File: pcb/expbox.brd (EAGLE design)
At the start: 87 x 47 mm, 48 parts, among them IC1 7805TV, K1 G5LE, Q1 2N3904, Q2 2N3904, Q3 2N3904, Q4 2N3904, Q5 2N3904, Q6 2N3904

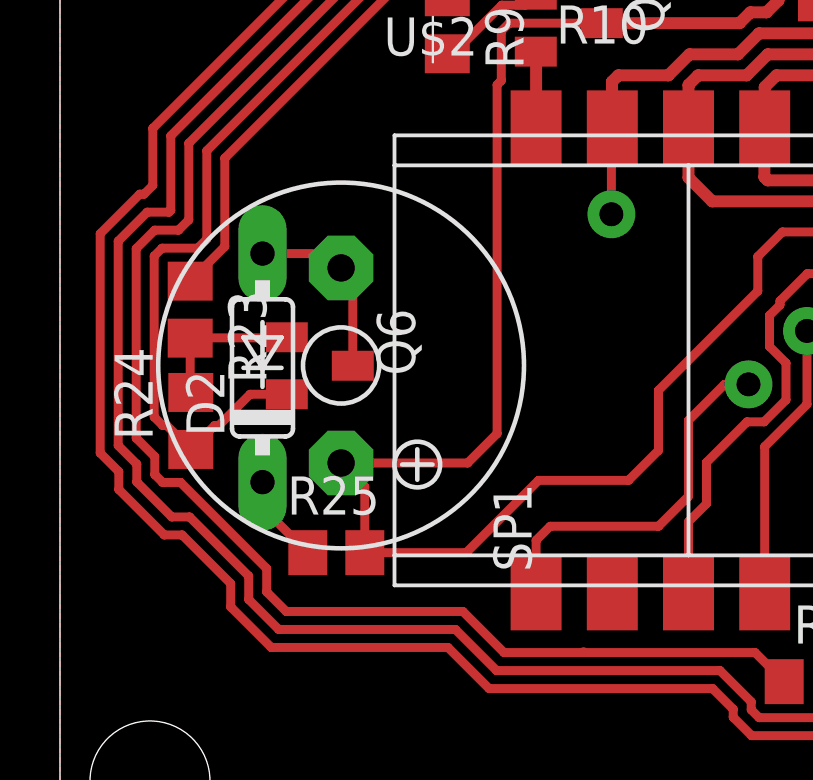
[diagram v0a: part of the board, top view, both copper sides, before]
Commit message: Replace buzzer with one with wider legs
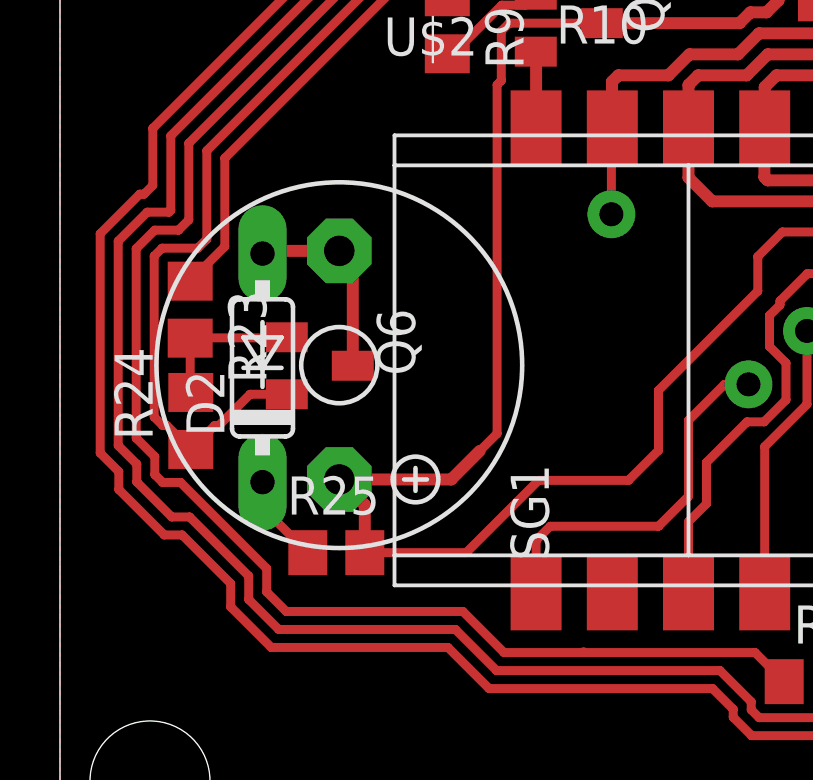
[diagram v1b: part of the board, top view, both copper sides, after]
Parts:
- removed SP1: KSS1201, buzzer:KSS1201
- added SG1: F/TMB, buzzer:F/TMB
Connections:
- net N$21: now also SG1.-; no longer SP1.-
- net VCC: now also SG1.+; no longer SP1.+
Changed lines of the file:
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@@
 <layer number="43" name="vRestrict" color="2" fill="10" visible="no" active="yes"/>
 <layer number="44" name="Drills" color="7" fill="1" visible="no" active="yes"/>
-<layer number="45" name="Holes" color="7" fill="1" visible="no" active="yes"/>
+<layer number="45" name="Holes" color="7" fill="1" visible="yes" active="yes"/>
 <layer number="46" name="Milling" color="3" fill="1" visible="no" active="yes"/>
 <layer number="47" name="Measures" color="7" fill="1" visible="no" active="yes"/>
@@
 <attribute name="VALUE" x="10.37" y="28.825" size="1.27" layer="27" rot="R270"/>
 </element>
-<element name="SP1" library="buzzer" library_urn="urn:adsk.eagle:library:113" package="KSS1201" package3d_urn="urn:adsk.eagle:package:5268/1" value="KSS1201" x="9.37" y="16.85" smashed="yes" rot="R270">
-<attribute name="MF" value="" x="-60.48" y="-30.14" size="1.778" layer="27" rot="R270" display="off"/>
-<attribute name="MPN" value="" x="-60.48" y="-30.14" size="1.778" layer="27" rot="R270" display="off"/>
-<attribute name="NAME" x="14.45" y="12.913" size="1.27" layer="25" ratio="10" rot="R270"/>
-<attribute name="OC_FARNELL" value="unknown" x="-60.48" y="-30.14" size="1.778" layer="27" rot="R270" display="off"/>
-<attribute name="OC_NEWARK" value="unknown" x="-60.48" y="-30.14" size="1.778" layer="27" rot="R270" display="off"/>
-<attribute name="POPULARITY" value="1" x="-60.48" y="-30.14" size="1.778" layer="27" rot="R270" display="off"/>
-<attribute name="VALUE" x="5.56" y="20.406" size="1.27" layer="27" ratio="10" rot="R270"/>
-</element>
 <element name="U$1" library="PIC16F886-I_SP" package="DIP762W46P254L3467H457Q28" value="PIC16F886-I/SP" x="31.95" y="38.02" smashed="yes" rot="MR90">
 <attribute name="AVAILABILITY" value="Good" x="0.2" y="65.96" size="1.778" layer="28" rot="MR90" display="off"/>
@@
 <attribute name="POPULARITY" value="10" x="149.58" y="76.85" size="1.778" layer="27" rot="R90" display="off"/>
 <attribute name="VALUE" x="87.985" y="3.19" size="1.27" layer="27" ratio="10" rot="R90"/>
+</element>
+<element name="SG1" library="buzzer" library_urn="urn:adsk.eagle:library:113" package="F/TMB" package3d_urn="urn:adsk.eagle:package:5260/1" value="F/TMB" x="9.31" y="16.86" smashed="yes" rot="R270">
+<attribute name="MF" value="" x="9.31" y="16.86" size="1.778" layer="27" rot="R270" display="off"/>
+<attribute name="MPN" value="" x="9.31" y="16.86" size="1.778" layer="27" rot="R270" display="off"/>
+<attribute name="NAME" x="15.025" y="13.558" size="1.27" layer="25" ratio="10" rot="R270"/>
+<attribute name="OC_FARNELL" value="unknown" x="9.31" y="16.86" size="1.778" layer="27" rot="R270" display="off"/>
+<attribute name="OC_NEWARK" value="unknown" x="9.31" y="16.86" size="1.778" layer="27" rot="R270" display="off"/>
+<attribute name="POPULARITY" value="1" x="9.31" y="16.86" size="1.778" layer="27" rot="R270" display="off"/>
+<attribute name="VALUE" x="5.5" y="20.67" size="1.27" layer="27" ratio="10" rot="R270"/>
 </element>
 </elements>
@@
 <vertex x="87" y="47"/>
 </polygon>
-<wire x1="31.77" y1="13.62" x2="31.77" y2="9.31" width="0" layer="19" extent="1-1"/>
+<wire x1="31.77" y1="9.31" x2="31.77" y2="13.62" width="0" layer="19" extent="1-1"/>
 </signal>
 <signal name="VCC">
@@
 <contactref element="K1" pad="1"/>
 <contactref element="D1" pad="C"/>
-<contactref element="SP1" pad="+"/>
 <contactref element="R25" pad="2"/>
 <wire x1="63" y1="31.28" x2="63" y2="33.23" width="0.5" layer="1"/>
@@
 <wire x1="28.14" y1="36.28" x2="28.14" y2="39.02" width="0.4" layer="1"/>
 <wire x1="28.14" y1="39.02" x2="28.14" y2="41.83" width="0.4" layer="1"/>
-<wire x1="10.16" y1="10.61" x2="10.16" y2="12.8088" width="0.3" layer="1"/>
-<wire x1="10.16" y1="12.8088" x2="9.37" y2="13.5988" width="0.3" layer="1"/>
 <wire x1="10.16" y1="10.61" x2="13.54" y2="10.61" width="0.3" layer="1"/>
 <wire x1="13.54" y1="10.61" x2="15.95" y2="13.02" width="0.3" layer="1"/>
@@
 <wire x1="14.71" y1="26.34639375" x2="14.57" y2="26.20639375" width="0.3" layer="1"/>
 <wire x1="14.57" y1="26.20639375" x2="14.57" y2="14.58" width="0.3" layer="1"/>
-<wire x1="13.5888" y1="13.5988" x2="9.37" y2="13.5988" width="0.3" layer="1"/>
 <wire x1="14.71" y1="27.99639375" x2="14.71" y2="26.34639375" width="0.3" layer="1"/>
-<wire x1="14.57" y1="14.58" x2="13.5888" y2="13.5988" width="0.3" layer="1"/>
+<wire x1="14.57" y1="14.58" x2="13.995" y2="14.005" width="0.3" layer="1"/>
+<wire x1="13.995" y1="14.005" x2="13.5888" y2="13.5988" width="0.3" layer="1"/>
 <wire x1="38.84639375" y1="5.84" x2="39.11" y2="6.10360625" width="0.3" layer="1"/>
 <wire x1="39.11" y1="6.10360625" x2="39.11" y2="6.73" width="0.3" layer="1"/>
@@
 <wire x1="73.67" y1="38.736" x2="69.406" y2="38.736" width="0.5" layer="1"/>
 <wire x1="69.406" y1="38.736" x2="67.85" y2="37.18" width="0.5" layer="1"/>
+<contactref element="SG1" pad="+"/>
+<wire x1="9.31" y1="13.05" x2="10.16" y2="12.2" width="0.4" layer="1"/>
+<wire x1="10.16" y1="12.2" x2="10.16" y2="10.61" width="0.4" layer="1"/>
+<wire x1="9.31" y1="13.05" x2="13.04" y2="13.05" width="0.4" layer="1"/>
+<wire x1="13.04" y1="13.05" x2="13.995" y2="14.005" width="0.4" layer="1"/>
 <wire x1="29.4" y1="35.05" x2="38.28" y2="39.21" width="0" layer="19" extent="1-1"/>
 </signal>
@@
 <signal name="N$21">
 <contactref element="Q6" pad="C"/>
-<contactref element="SP1" pad="-"/>
 <contactref element="D2" pad="A"/>
-<wire x1="9.37" y1="20.1012" x2="8.8912" y2="20.58" width="0.3" layer="1"/>
-<wire x1="8.8912" y1="20.58" x2="6.75" y2="20.58" width="0.3" layer="1"/>
-<wire x1="9.37" y1="20.1012" x2="9.76" y2="19.7112" width="0.3" layer="1"/>
-<wire x1="9.76" y1="19.7112" x2="9.76" y2="16.84" width="0.3" layer="1"/>
+<contactref element="SG1" pad="-"/>
+<wire x1="6.75" y1="20.58" x2="6.84" y2="20.67" width="0.4" layer="1"/>
+<wire x1="6.84" y1="20.67" x2="9.31" y2="20.67" width="0.4" layer="1"/>
+<wire x1="9.31" y1="20.67" x2="9.76" y2="20.22" width="0.4" layer="1"/>
+<wire x1="9.76" y1="20.22" x2="9.76" y2="16.84" width="0.4" layer="1"/>
 </signal>
 <signal name="N$24">
